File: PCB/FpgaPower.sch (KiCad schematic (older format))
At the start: 11 parts, among them U5 10CLxxxYE144

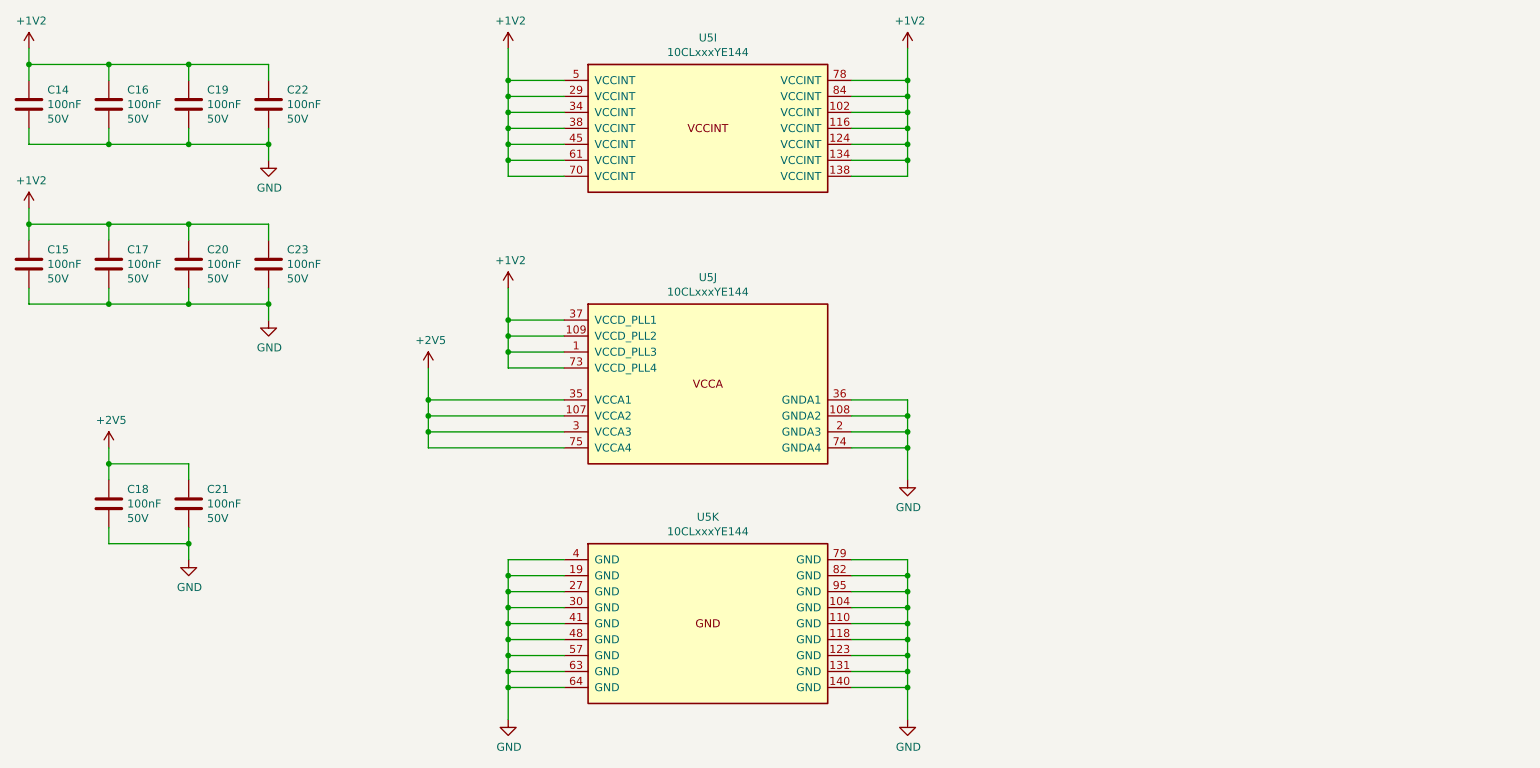
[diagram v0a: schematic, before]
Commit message: Connect the FPGA configuration signals
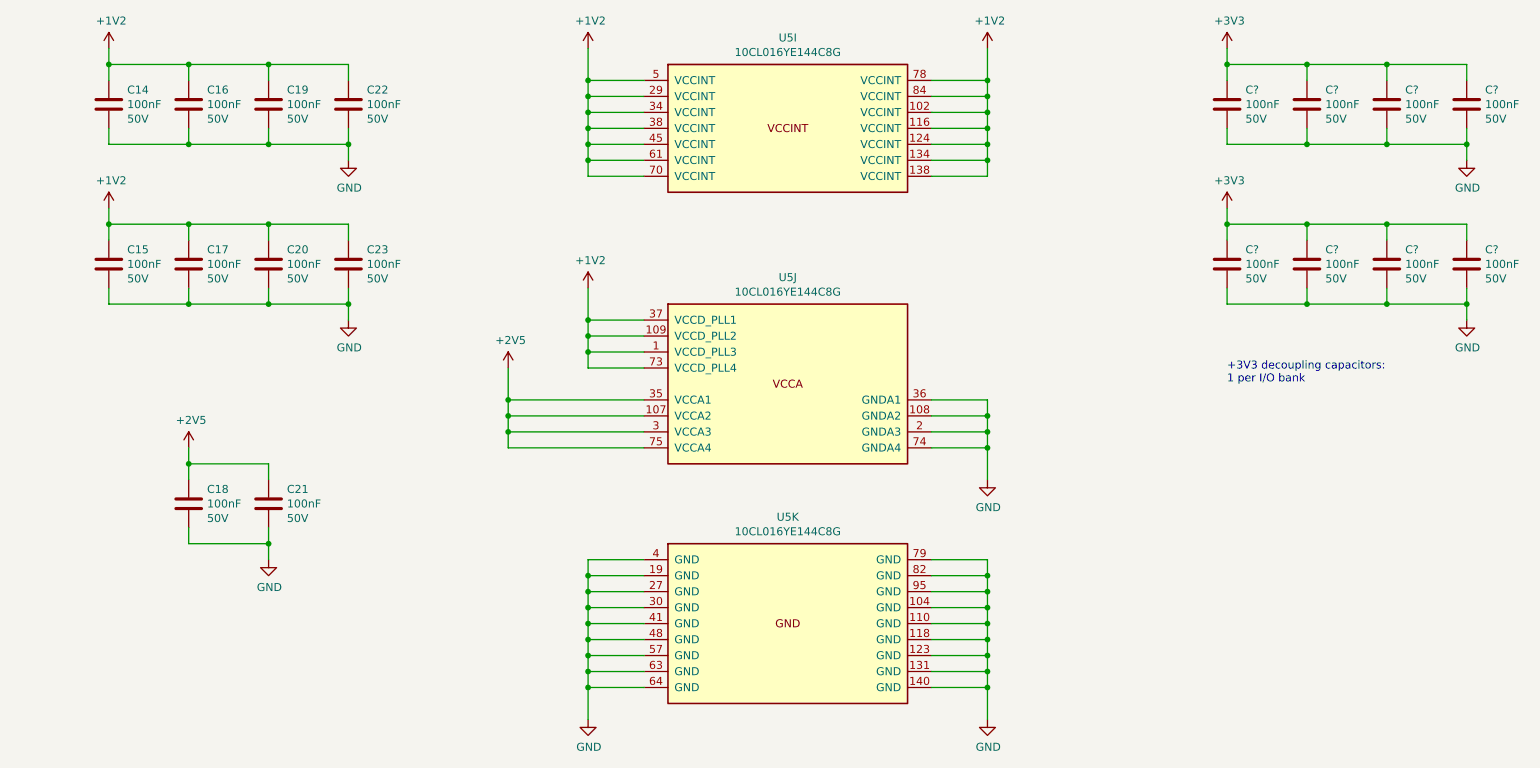
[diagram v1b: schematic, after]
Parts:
- added C? (x8): 100nF, Capacitor_SMD:C_0603_1608Metric, symbol Device:C
- C14, C15, C16, C17, C18, C19, C20, C21, C22, C23: Part_Number C1608X5R1H104K080AA -> (none); Part_number (none) -> C1608X5R1H104K080AA
- U5: value 10CLxxxYE144 -> 10CL016YE144C8G; Part_number (none) -> 10CL016YE144C8G
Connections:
- net GND: now also C?.2, C?.2, C?.2, C?.2, C?.2, C?.2, C?.2, C?.2
- new net +3V3: C?.1, C?.1, C?.1, C?.1, C?.1, C?.1, C?.1, C?.1
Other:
- note added: "+3V3 decoupling capacitors:\n1 per I/O bank"
- moved on the sheet: C14, C15, C16, C17, C18, C19, C20, C21, C22, C23, U5I, U5J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
